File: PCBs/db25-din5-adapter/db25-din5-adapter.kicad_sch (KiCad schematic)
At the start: 4 parts, among them J1 DB25_Plug_MountingHoles, J2 TX/RX Straight/cross, J3 DTR/RTS Straight/cross

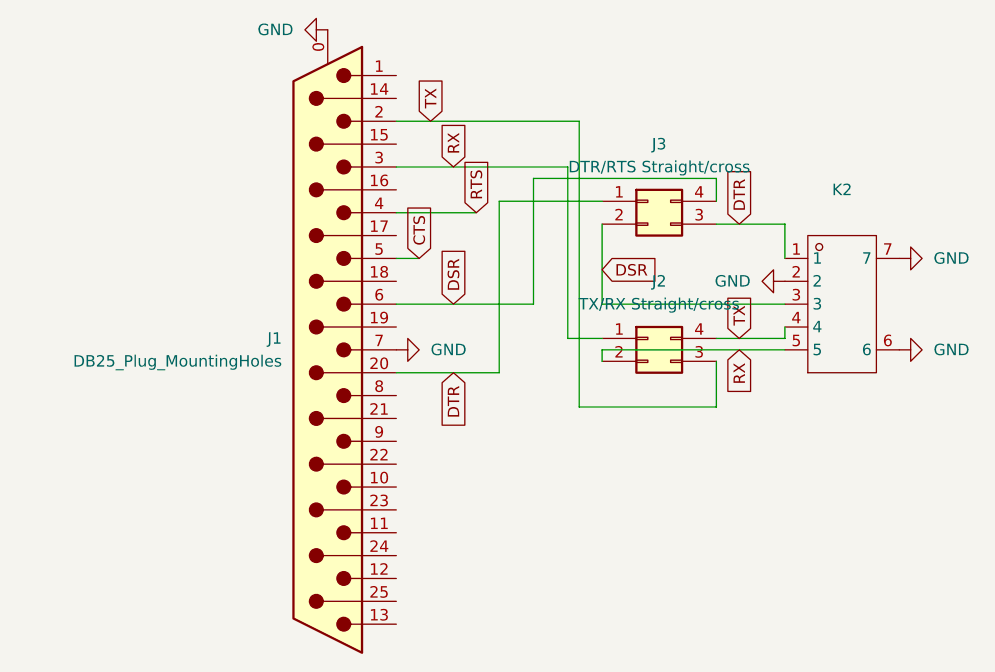
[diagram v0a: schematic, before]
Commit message: Update Quicktake doc and PCBs
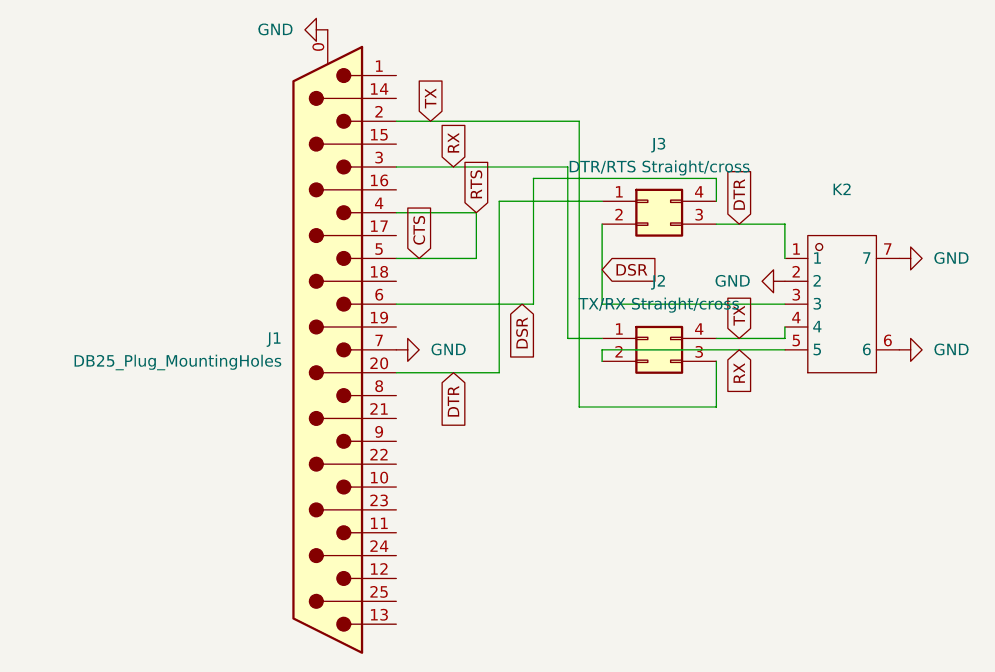
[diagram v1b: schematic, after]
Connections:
- net RTS is gone; now on net CTS: J1.4
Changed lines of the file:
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@@
-	(wire
-		(pts
-			(xy 106.68 67.31) (xy 109.22 67.31)
-		)
-		(stroke
-			(width 0)
-			(type default)
-		)
-	)
 	(wire
 		(pts
@@
 	(wire
 		(pts
+			(xy 115.57 62.23) (xy 115.57 67.31)
+		)
+		(stroke
+			(width 0)
+			(type default)
+		)
+	)
+	(wire
+		(pts
 			(xy 129.54 72.39) (xy 149.86 72.39)
 		)
@@
 	(wire
 		(pts
+			(xy 106.68 67.31) (xy 115.57 67.31)
+		)
+		(stroke
+			(width 0)
+			(type default)
+		)
+	)
+	(wire
+		(pts
 			(xy 142.24 76.2) (xy 149.86 76.2)
 		)
@@
 	(global_label "DSR"
 		(shape input)
-		(at 113.03 72.39 90)
-		(fields_autoplaced yes)
-		(effects
-			(font
-				(size 1.27 1.27)
-			)
-			(justify left)
-		)
-		(property "Intersheetrefs" "${INTERSHEET_REFS}"
-			(at 113.03 65.6553 90)
-			(effects
-				(font
-					(size 1.27 1.27)
-				)
-				(justify left)
+		(at 120.65 72.39 270)
+		(fields_autoplaced yes)
+		(effects
+			(font
+				(size 1.27 1.27)
+			)
+			(justify right)
+		)
+		(property "Intersheetrefs" "${INTERSHEET_REFS}"
+			(at 120.65 79.1247 90)
+			(effects
+				(font
+					(size 1.27 1.27)
+				)
+				(justify right)
 				(hide yes)
 			)
@@
 		)
 		(instances
-			(project ""
+			(project "db25-din5-adapter"
 				(path "/7108ec36-da4c-4f22-b5ad-0a42d2aa000b"
 					(reference "J1")
